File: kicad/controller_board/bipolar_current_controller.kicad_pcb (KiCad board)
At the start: 4 copper layers, 114.3 x 127 mm, 131 parts, among them J1 Error signal, J2 Set point, J4 Monitor, J5 Conn_02x04_Counter_Clockwise, J6 Enable, J7 N-MOS, J8 P-MOS, J9 Shunt resistor, P1 CONN_01X03, U1 AD8421, U11 LM338, U12 LM337_TO220, U13 LM7915, U14 uA7815, U15 LM7905, U16 LM7805, U17 TL1963A, U18 LM337_TO220, U19 FOD8482TR2, U2 AD8421, U3 AD8421, U4 OPA388, U5 LT1363, U6 LT1363, U7 BUF634A, U8 BUF634A

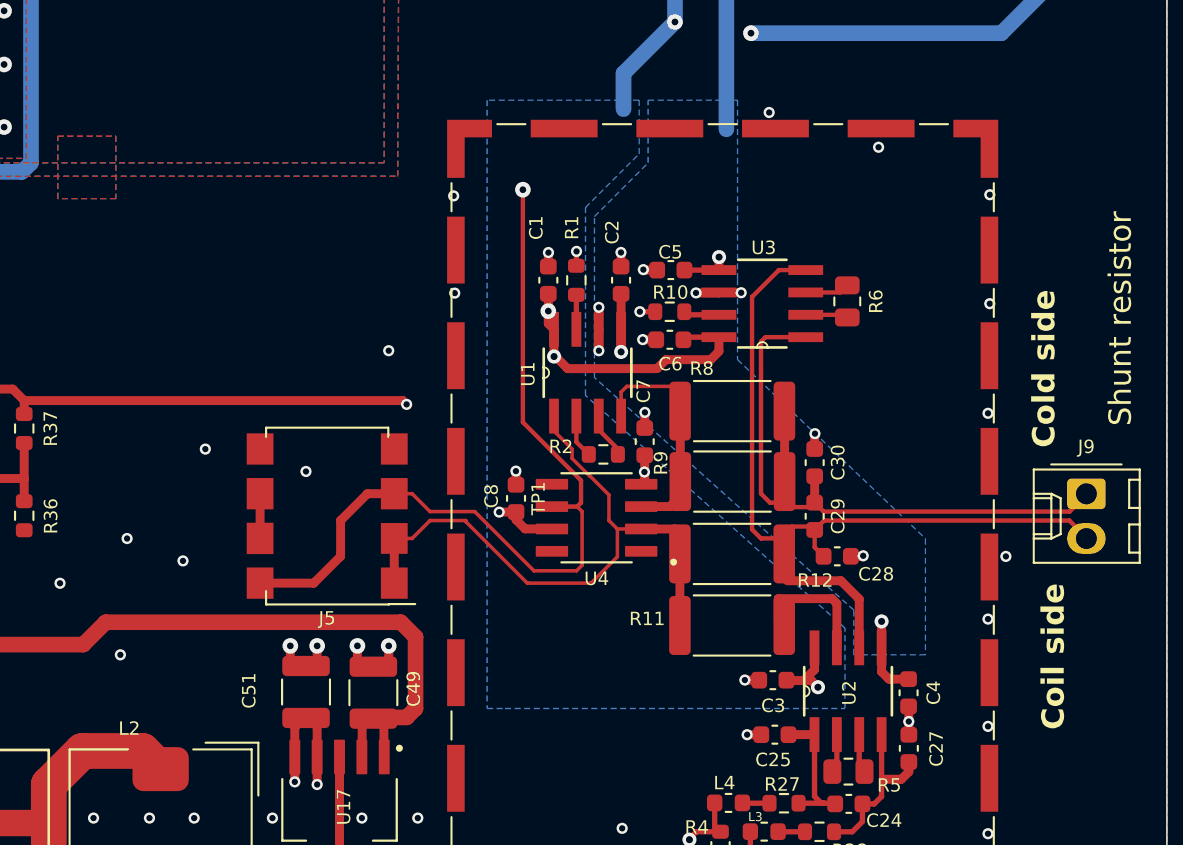
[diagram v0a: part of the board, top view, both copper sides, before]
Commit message: Fixing wrong labels and adding silkscreen
While testing the board we discovered a wrong labeling for the
 shunt resistor terminals. The board layout is not affected by
 the wrong labeling but a silkscreen needed to be moved.

The schematic was also updated showing a clearer (and correct) labeling.

Additionally I added a legend to the board silkscreen showing the
pinout of the DIL socket.
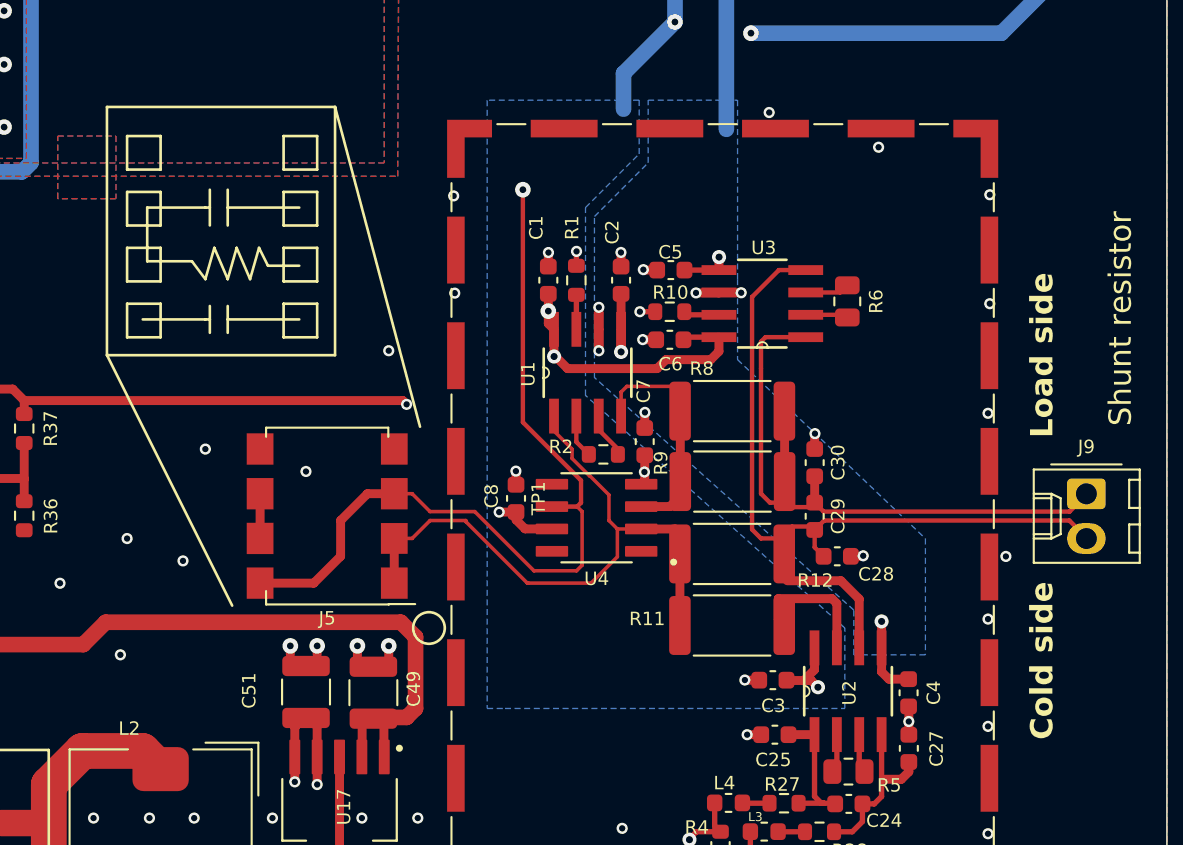
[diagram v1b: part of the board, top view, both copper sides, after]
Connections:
- net POWER_GND_REF renamed Hot_side
- net U2 renamed Power_gnd_ref
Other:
- board text added: "Load side"
- board text removed: "Coil side"
